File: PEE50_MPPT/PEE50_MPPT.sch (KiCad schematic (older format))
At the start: 46 parts, among them J1 PV_IN1, J2 PV_IN2, J3 Conn_01x02_Female, J4 Conn_01x02_Female, J5 PV_IN4, J6 PV_IN3, Q1 BC547, Q2 BC547, Q3 BC547, Q4 BC547, U1 LM3480-3.3

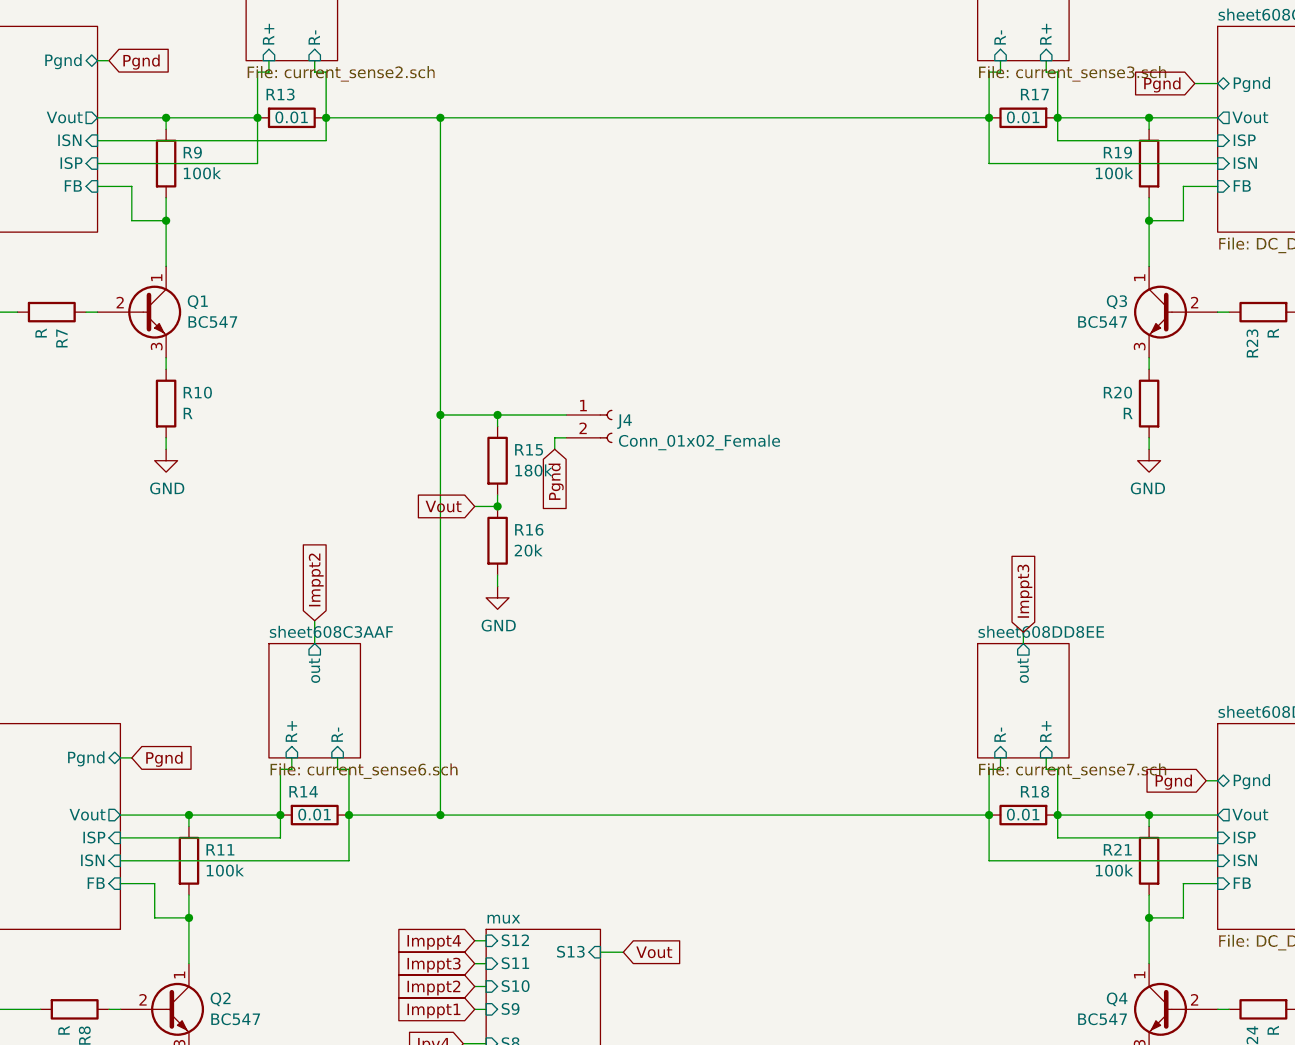
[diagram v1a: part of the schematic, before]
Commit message: best veel footprints ingevoegd
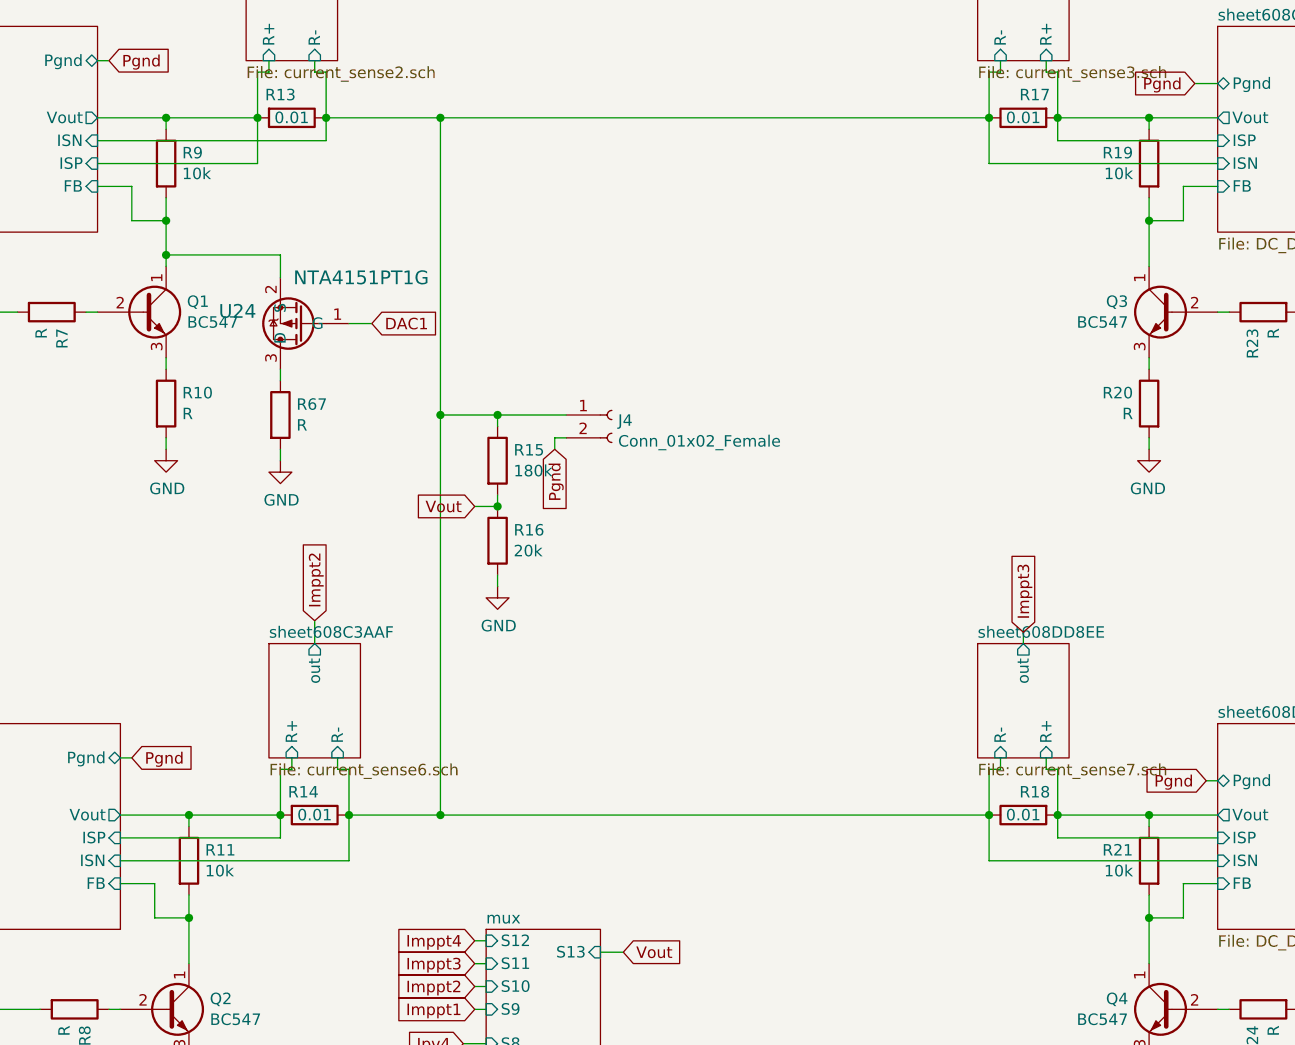
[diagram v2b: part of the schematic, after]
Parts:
- added R67: R, Resistor_SMD:R_1206_3216Metric_Pad1.42x1.75mm_HandSolder, symbol Device:R
- added U24: NTA4151PT1G, SOT416_463_ONS, symbol Robin_lib:NTA4151PT1G
- C1, C2, C57, C58: footprint (none) -> Capacitor_SMD:C_1206_3216Metric_Pad1.42x1.75mm_HandSolder
- JP1: footprint (none) -> Connector_PinHeader_2.54mm:PinHeader_1x03_P2.54mm_Vertical
- R1, R10, R12, R15, R16, R2, R20, R22, R23, R24, R27, R28, R29, R3, R30, R4, R7, R8: footprint (none) -> Resistor_SMD:R_1206_3216Metric_Pad1.42x1.75mm_HandSolder
- R11, R19, R21, R9: value 100k -> 10k; footprint (none) -> Resistor_SMD:R_1206_3216Metric_Pad1.42x1.75mm_HandSolder
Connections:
- net DAC1: now also U24.1 (G)
- net DC/DC_Converter/FB: now also U24.2 (S)
- net GND: now also R67.2
- new net: R67.1, U24.3 (D)
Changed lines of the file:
@@
 EESchema Schematic File Version 4
-LIBS:PEE50_MPPT-cache
-EELAYER 26 0
+EELAYER 30 0
 EELAYER END
 $Descr A4 11693 8268
@@
 P 2900 1950
 F 0 "R9" H 2970 1996 50  0000 L CNN
-F 1 "100k" H 2970 1905 50  0000 L CNN
-F 2 "" V 2830 1950 50  0001 C CNN
+F 1 "10k" H 2970 1905 50  0000 L CNN
+F 2 "Resistor_SMD:R_1206_3216Metric_Pad1.42x1.75mm_HandSolder" V 2830 1950 50  0001 C CNN
 F 3 "~" H 2900 1950 50  0001 C CNN
 	1    2900 1950
@@
 Connection ~ 2900 2200
 Wire Wire Line
-	2900 2200 2900 2400
+	2900 2200 2900 2350
 $Comp
 L Device:R R10
@@
 F 0 "R10" H 2970 3046 50  0000 L CNN
 F 1 "R" H 2970 2955 50  0000 L CNN
-F 2 "" V 2830 3000 50  0001 C CNN
+F 2 "Resistor_SMD:R_1206_3216Metric_Pad1.42x1.75mm_HandSolder" V 2830 3000 50  0001 C CNN
 F 3 "~" H 2900 3000 50  0001 C CNN
 	1    2900 3000
@@
 F 0 "R1" H 1020 2096 50  0000 L CNN
 F 1 "180k" H 1020 2005 50  0000 L CNN
-F 2 "" V 880 2050 50  0001 C CNN
+F 2 "Resistor_SMD:R_1206_3216Metric_Pad1.42x1.75mm_HandSolder" V 880 2050 50  0001 C CNN
 F 3 "~" H 950 2050 50  0001 C CNN
 	1    950  2050
@@
 F 0 "R2" H 1020 2446 50  0000 L CNN
 F 1 "20k" H 1020 2355 50  0000 L CNN
-F 2 "" V 880 2400 50  0001 C CNN
+F 2 "Resistor_SMD:R_1206_3216Metric_Pad1.42x1.75mm_HandSolder" V 880 2400 50  0001 C CNN
 F 3 "~" H 950 2400 50  0001 C CNN
 	1    950  2400
@@
 F 0 "R7" H 2470 2646 50  0000 L CNN
 F 1 "R" H 2470 2555 50  0000 L CNN
-F 2 "" V 2330 2600 50  0001 C CNN
+F 2 "Resistor_SMD:R_1206_3216Metric_Pad1.42x1.75mm_HandSolder" V 2330 2600 50  0001 C CNN
 F 3 "~" H 2400 2600 50  0001 C CNN
 	1    2400 2600
@@
 F 0 "R15" H 4420 3296 50  0000 L CNN
 F 1 "180k" H 4420 3205 50  0000 L CNN
-F 2 "" V 4280 3250 50  0001 C CNN
+F 2 "Resistor_SMD:R_1206_3216Metric_Pad1.42x1.75mm_HandSolder" V 4280 3250 50  0001 C CNN
 F 3 "~" H 4350 3250 50  0001 C CNN
 	1    4350 3250
@@
 F 0 "R16" H 4420 3646 50  0000 L CNN
 F 1 "20k" H 4420 3555 50  0000 L CNN
-F 2 "" V 4280 3600 50  0001 C CNN
+F 2 "Resistor_SMD:R_1206_3216Metric_Pad1.42x1.75mm_HandSolder" V 4280 3600 50  0001 C CNN
 F 3 "~" H 4350 3600 50  0001 C CNN
 	1    4350 3600
@@
 P 3000 5000
 F 0 "R11" H 3070 5046 50  0000 L CNN
-F 1 "100k" H 3070 4955 50  0000 L CNN
-F 2 "" V 2930 5000 50  0001 C CNN
+F 1 "10k" H 3070 4955 50  0000 L CNN
+F 2 "Resistor_SMD:R_1206_3216Metric_Pad1.42x1.75mm_HandSolder" V 2930 5000 50  0001 C CNN
 F 3 "~" H 3000 5000 50  0001 C CNN
 	1    3000 5000
@@
 F 0 "R12" H 3070 6096 50  0000 L CNN
 F 1 "R" H 3070 6005 50  0000 L CNN
-F 2 "" V 2930 6050 50  0001 C CNN
+F 2 "Resistor_SMD:R_1206_3216Metric_Pad1.42x1.75mm_HandSolder" V 2930 6050 50  0001 C CNN
 F 3 "~" H 3000 6050 50  0001 C CNN
 	1    3000 6050
@@
 F 0 "R3" H 1120 5146 50  0000 L CNN
 F 1 "180k" H 1120 5055 50  0000 L CNN
-F 2 "" V 980 5100 50  0001 C CNN
+F 2 "Resistor_SMD:R_1206_3216Metric_Pad1.42x1.75mm_HandSolder" V 980 5100 50  0001 C CNN
 F 3 "~" H 1050 5100 50  0001 C CNN
 	1    1050 5100
@@
 F 0 "R4" H 1120 5496 50  0000 L CNN
 F 1 "20k" H 1120 5405 50  0000 L CNN
-F 2 "" V 980 5450 50  0001 C CNN
+F 2 "Resistor_SMD:R_1206_3216Metric_Pad1.42x1.75mm_HandSolder" V 980 5450 50  0001 C CNN
 F 3 "~" H 1050 5450 50  0001 C CNN
 	1    1050 5450
@@
 F 0 "R8" H 2570 5696 50  0000 L CNN
 F 1 "R" H 2570 5605 50  0000 L CNN
-F 2 "" V 2430 5650 50  0001 C CNN
+F 2 "Resistor_SMD:R_1206_3216Metric_Pad1.42x1.75mm_HandSolder" V 2430 5650 50  0001 C CNN
 F 3 "~" H 2500 5650 50  0001 C CNN
 	1    2500 5650
@@
 P 7200 1950
 F 0 "R19" H 7270 1996 50  0000 L CNN
-F 1 "100k" H 7270 1905 50  0000 L CNN
-F 2 "" V 7130 1950 50  0001 C CNN
+F 1 "10k" H 7270 1905 50  0000 L CNN
+F 2 "Resistor_SMD:R_1206_3216Metric_Pad1.42x1.75mm_HandSolder" V 7130 1950 50  0001 C CNN
 F 3 "~" H 7200 1950 50  0001 C CNN
 	1    7200 1950
@@
 F 0 "R20" H 7270 3046 50  0000 L CNN
 F 1 "R" H 7270 2955 50  0000 L CNN
-F 2 "" V 7130 3000 50  0001 C CNN
+F 2 "Resistor_SMD:R_1206_3216Metric_Pad1.42x1.75mm_HandSolder" V 7130 3000 50  0001 C CNN
 F 3 "~" H 7200 3000 50  0001 C CNN
 	1    7200 3000
@@
 F 0 "R27" H 9220 2096 50  0000 L CNN
 F 1 "180k" H 9220 2005 50  0000 L CNN
-F 2 "" V 9080 2050 50  0001 C CNN
+F 2 "Resistor_SMD:R_1206_3216Metric_Pad1.42x1.75mm_HandSolder" V 9080 2050 50  0001 C CNN
 F 3 "~" H 9150 2050 50  0001 C CNN
 	1    9150 2050
@@
 F 0 "R28" H 9220 2446 50  0000 L CNN
 F 1 "20k" H 9220 2355 50  0000 L CNN
-F 2 "" V 9080 2400 50  0001 C CNN
+F 2 "Resistor_SMD:R_1206_3216Metric_Pad1.42x1.75mm_HandSolder" V 9080 2400 50  0001 C CNN
 F 3 "~" H 9150 2400 50  0001 C CNN
 	1    9150 2400
@@
 F 0 "R23" H 7770 2646 50  0000 L CNN
 F 1 "R" H 7770 2555 50  0000 L CNN
-F 2 "" V 7630 2600 50  0001 C CNN
+F 2 "Resistor_SMD:R_1206_3216Metric_Pad1.42x1.75mm_HandSolder" V 7630 2600 50  0001 C CNN
 F 3 "~" H 7700 2600 50  0001 C CNN
 	1    7700 2600
@@
 P 7200 5000
 F 0 "R21" H 7270 5046 50  0000 L CNN
-F 1 "100k" H 7270 4955 50  0000 L CNN
-F 2 "" V 7130 5000 50  0001 C CNN
+F 1 "10k" H 7270 4955 50  0000 L CNN
+F 2 "Resistor_SMD:R_1206_3216Metric_Pad1.42x1.75mm_HandSolder" V 7130 5000 50  0001 C CNN
 F 3 "~" H 7200 5000 50  0001 C CNN
 	1    7200 5000
@@
 F 0 "R22" H 7270 6096 50  0000 L CNN
 F 1 "R" H 7270 6005 50  0000 L CNN
-F 2 "" V 7130 6050 50  0001 C CNN
+F 2 "Resistor_SMD:R_1206_3216Metric_Pad1.42x1.75mm_HandSolder" V 7130 6050 50  0001 C CNN
 F 3 "~" H 7200 6050 50  0001 C CNN
 	1    7200 6050
@@
 F 0 "R29" H 9220 5146 50  0000 L CNN
 F 1 "180k" H 9220 5055 50  0000 L CNN
-F 2 "" V 9080 5100 50  0001 C CNN
+F 2 "Resistor_SMD:R_1206_3216Metric_Pad1.42x1.75mm_HandSolder" V 9080 5100 50  0001 C CNN
 F 3 "~" H 9150 5100 50  0001 C CNN
 	1    9150 5100
@@
 F 0 "R30" H 9220 5496 50  0000 L CNN
 F 1 "20k" H 9220 5405 50  0000 L CNN
-F 2 "" V 9080 5450 50  0001 C CNN
+F 2 "Resistor_SMD:R_1206_3216Metric_Pad1.42x1.75mm_HandSolder" V 9080 5450 50  0001 C CNN
 F 3 "~" H 9150 5450 50  0001 C CNN
 	1    9150 5450
@@
 F 0 "R24" H 7770 5696 50  0000 L CNN
 F 1 "R" H 7770 5605 50  0000 L CNN
-F 2 "" V 7630 5650 50  0001 C CNN
+F 2 "Resistor_SMD:R_1206_3216Metric_Pad1.42x1.75mm_HandSolder" V 7630 5650 50  0001 C CNN
 F 3 "~" H 7700 5650 50  0001 C CNN
 	1    7700 5650
@@
 F 0 "JP1" V 2046 7252 50  0000 L CNN
 F 1 "Jumper_NC_Dual" V 1955 7252 50  0000 L CNN
-F 2 "" H 2000 7150 50  0001 C CNN
+F 2 "Connector_PinHeader_2.54mm:PinHeader_1x03_P2.54mm_Vertical" H 2000 7150 50  0001 C CNN
 F 3 "~" H 2000 7150 50  0001 C CNN
 	1    2000 7150
@@
 F 0 "C1" H 2215 6846 50  0000 L CNN
 F 1 "1u" H 2215 6755 50  0000 L CNN
-F 2 "" H 2138 6650 50  0001 C CNN
+F 2 "Capacitor_SMD:C_1206_3216Metric_Pad1.42x1.75mm_HandSolder" H 2138 6650 50  0001 C CNN
 F 3 "~" H 2100 6800 50  0001 C CNN
 	1    2100 6800
@@
 F 0 "C2" H 2915 6846 50  0000 L CNN
 F 1 "100n" H 2915 6755 50  0000 L CNN
-F 2 "" H 2838 6650 50  0001 C CNN
+F 2 "Capacitor_SMD:C_1206_3216Metric_Pad1.42x1.75mm_HandSolder" H 2838 6650 50  0001 C CNN
 F 3 "~" H 2800 6800 50  0001 C CNN
 	1    2800 6800
@@
 F 0 "C57" H 1865 7646 50  0000 L CNN
 F 1 "1u" H 1865 7555 50  0000 L CNN
-F 2 "" H 1788 7450 50  0001 C CNN
+F 2 "Capacitor_SMD:C_1206_3216Metric_Pad1.42x1.75mm_HandSolder" H 1788 7450 50  0001 C CNN
 F 3 "~" H 1750 7600 50  0001 C CNN
 	1    1750 7600
@@
 F 0 "C58" H 2115 7646 50  0000 L CNN
 F 1 "100n" H 2115 7555 50  0000 L CNN
-F 2 "" H 2038 7450 50  0001 C CNN
+F 2 "Capacitor_SMD:C_1206_3216Metric_Pad1.42x1.75mm_HandSolder" H 2038 7450 50  0001 C CNN
 F 3 "~" H 2000 7600 50  0001 C CNN
 	1    2000 7600
@@
 	1    0    0    -1
 $EndComp
+$Comp
+L Robin_lib:NTA4151PT1G U24
+U 1 1 6095AD8A
+P 4200 2700
+F 0 "U24" H 5105 2597 60  0000 L CNN
+F 1 "NTA4151PT1G" H 4350 2450 60  0000 L CNN
+F 2 "SOT416_463_ONS" H 5000 2940 60  0001 C CNN
+F 3 "" H 4200 2700 60  0000 C CNN
+	1    4200 2700
+	-1   0    0    1
+$EndComp
+Wire Wire Line
+	3400 2450 3400 2350
+Wire Wire Line
+	3400 2350 2900 2350
+Connection ~ 2900 2350
+Wire Wire Line
+	2900 2350 2900 2400
+$Comp
+L Device:R R67
+U 1 1 6096B3EE
+P 3400 3050
+F 0 "R67" H 3470 3096 50  0000 L CNN
+F 1 "R" H 3470 3005 50  0000 L CNN
+F 2 "Resistor_SMD:R_1206_3216Metric_Pad1.42x1.75mm_HandSolder" V 3330 3050 50  0001 C CNN
+F 3 "~" H 3400 3050 50  0001 C CNN
+	1    3400 3050
+	1    0    0    -1
+$EndComp
+$Comp
+L power:GND #PWR0104
+U 1 1 6096B7C0
+P 3400 3250
+F 0 "#PWR0104" H 3400 3000 50  0001 C CNN
+F 1 "GND" H 3405 3077 50  0000 C CNN
+F 2 "" H 3400 3250 50  0001 C CNN
+F 3 "" H 3400 3250 50  0001 C CNN
+	1    3400 3250
+	1    0    0    -1
+$EndComp
+Wire Wire Line
+	3400 3250 3400 3200
+Wire Wire Line
+	3400 2900 3400 2850
+Text GLabel 3800 2650 2    50   Input ~ 0
+DAC1
+Wire Wire Line
+	3800 2650 3700 2650
 $EndSCHEMATC

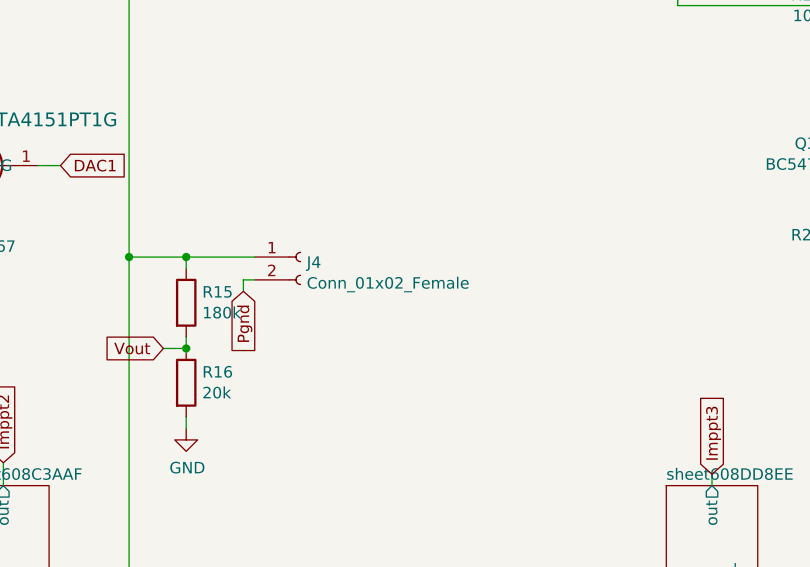
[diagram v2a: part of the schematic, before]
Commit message: footprints gemapt + 10x10 pcb rand getekend
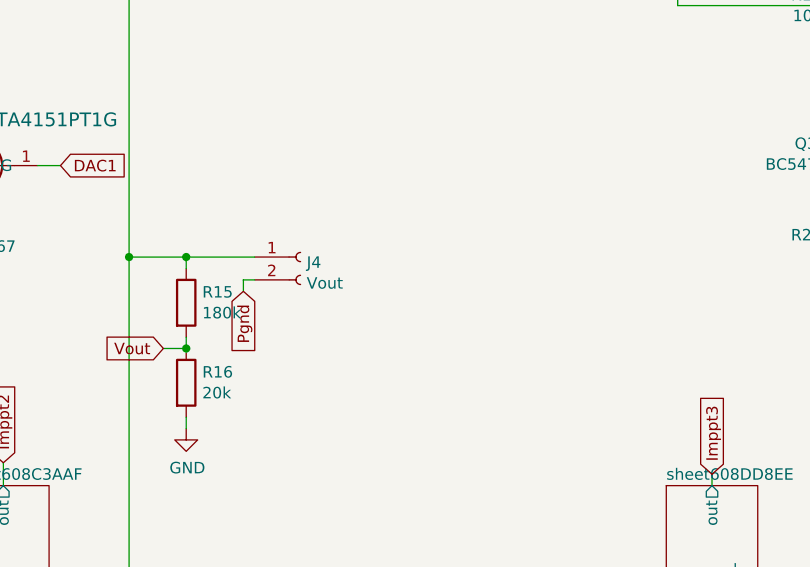
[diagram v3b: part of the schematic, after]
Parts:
- J1, J2, J5, J6: footprint (none) -> Connector_Phoenix_MSTB:PhoenixContact_MSTBA_2,5_2-G-5,08_1x02_P5.08mm_Horizontal
- J3: footprint (none) -> Connector_PinSocket_2.54mm:PinSocket_1x02_P2.54mm_Vertical
- J4: value Conn_01x02_Female -> Vout; footprint (none) -> Connector_Phoenix_MSTB:PhoenixContact_MSTBA_2,5_2-G-5,08_1x02_P5.08mm_Horizontal
- R13, R14, R17, R18, R25, R26, R5, R6: footprint (none) -> Resistor_SMD:R_2512_6332Metric_Pad1.52x3.35mm_HandSolder
- U24: footprint SOT416_463_ONS -> AudioProject:NTA4151PT1G
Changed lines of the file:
@@
 EESchema Schematic File Version 4
-EELAYER 30 0
+LIBS:PEE50_MPPT-cache
+EELAYER 26 0
 EELAYER END
 $Descr A4 11693 8268
@@
 F 0 "J1" H 594 1525 50  0000 C CNN
 F 1 "PV_IN1" H 594 1616 50  0000 C CNN
-F 2 "" H 700 1850 50  0001 C CNN
+F 2 "Connector_Phoenix_MSTB:PhoenixContact_MSTBA_2,5_2-G-5,08_1x02_P5.08mm_Horizontal" H 700 1850 50  0001 C CNN
 F 3 "~" H 700 1850 50  0001 C CNN
 	1    700  1850
@@
 F 0 "R5" V 1050 1700 50  0000 C CNN
 F 1 "0.01" V 1150 1750 50  0000 C CNN
-F 2 "" V 1080 1750 50  0001 C CNN
+F 2 "Resistor_SMD:R_2512_6332Metric_Pad1.52x3.35mm_HandSolder" V 1080 1750 50  0001 C CNN
 F 3 "~" H 1150 1750 50  0001 C CNN
 	1    1150 1750
@@
 F 0 "R13" V 3350 1700 50  0000 C CNN
 F 1 "0.01" V 3450 1750 50  0000 C CNN
-F 2 "" V 3380 1750 50  0001 C CNN
+F 2 "Resistor_SMD:R_2512_6332Metric_Pad1.52x3.35mm_HandSolder" V 3380 1750 50  0001 C CNN
 F 3 "~" H 3450 1750 50  0001 C CNN
 	1    3450 1750
@@
 P 4850 3050
 F 0 "J4" H 4877 3026 50  0000 L CNN
-F 1 "Conn_01x02_Female" H 4877 2935 50  0000 L CNN
-F 2 "" H 4850 3050 50  0001 C CNN
+F 1 "Vout" H 4877 2935 50  0000 L CNN
+F 2 "Connector_Phoenix_MSTB:PhoenixContact_MSTBA_2,5_2-G-5,08_1x02_P5.08mm_Horizontal" H 4850 3050 50  0001 C CNN
 F 3 "~" H 4850 3050 50  0001 C CNN
 	1    4850 3050
@@
 F 0 "J2" H 694 4575 50  0000 C CNN
 F 1 "PV_IN2" H 694 4666 50  0000 C CNN
-F 2 "" H 800 4900 50  0001 C CNN
+F 2 "Connector_Phoenix_MSTB:PhoenixContact_MSTBA_2,5_2-G-5,08_1x02_P5.08mm_Horizontal" H 800 4900 50  0001 C CNN
 F 3 "~" H 800 4900 50  0001 C CNN
 	1    800  4900
@@
 F 0 "R6" V 1150 4750 50  0000 C CNN
 F 1 "0.01" V 1250 4800 50  0000 C CNN
-F 2 "" V 1180 4800 50  0001 C CNN
+F 2 "Resistor_SMD:R_2512_6332Metric_Pad1.52x3.35mm_HandSolder" V 1180 4800 50  0001 C CNN
 F 3 "~" H 1250 4800 50  0001 C CNN
 	1    1250 4800
@@
 F 0 "R14" V 3450 4750 50  0000 C CNN
 F 1 "0.01" V 3550 4800 50  0000 C CNN
-F 2 "" V 3480 4800 50  0001 C CNN
+F 2 "Resistor_SMD:R_2512_6332Metric_Pad1.52x3.35mm_HandSolder" V 3480 4800 50  0001 C CNN
 F 3 "~" H 3550 4800 50  0001 C CNN
 	1    3550 4800
@@
 F 0 "J5" H 9294 1525 50  0000 C CNN
 F 1 "PV_IN4" H 9294 1616 50  0000 C CNN
-F 2 "" H 9400 1850 50  0001 C CNN
+F 2 "Connector_Phoenix_MSTB:PhoenixContact_MSTBA_2,5_2-G-5,08_1x02_P5.08mm_Horizontal" H 9400 1850 50  0001 C CNN
 F 3 "~" H 9400 1850 50  0001 C CNN
 	1    9400 1850
@@
 F 0 "R25" V 8850 1700 50  0000 C CNN
 F 1 "0.01" V 8950 1750 50  0000 C CNN
-F 2 "" V 8880 1750 50  0001 C CNN
+F 2 "Resistor_SMD:R_2512_6332Metric_Pad1.52x3.35mm_HandSolder" V 8880 1750 50  0001 C CNN
 F 3 "~" H 8950 1750 50  0001 C CNN
 	1    8950 1750
@@
 F 0 "R17" V 6550 1700 50  0000 C CNN
 F 1 "0.01" V 6650 1750 50  0000 C CNN
-F 2 "" V 6580 1750 50  0001 C CNN
+F 2 "Resistor_SMD:R_2512_6332Metric_Pad1.52x3.35mm_HandSolder" V 6580 1750 50  0001 C CNN
 F 3 "~" H 6650 1750 50  0001 C CNN
 	1    6650 1750
@@
 F 0 "J6" H 9294 4575 50  0000 C CNN
 F 1 "PV_IN3" H 9294 4666 50  0000 C CNN
-F 2 "" H 9400 4900 50  0001 C CNN
+F 2 "Connector_Phoenix_MSTB:PhoenixContact_MSTBA_2,5_2-G-5,08_1x02_P5.08mm_Horizontal" H 9400 4900 50  0001 C CNN
 F 3 "~" H 9400 4900 50  0001 C CNN
 	1    9400 4900
@@
 F 0 "R26" V 8850 4750 50  0000 C CNN
 F 1 "0.01" V 8950 4800 50  0000 C CNN
-F 2 "" V 8880 4800 50  0001 C CNN
+F 2 "Resistor_SMD:R_2512_6332Metric_Pad1.52x3.35mm_HandSolder" V 8880 4800 50  0001 C CNN
 F 3 "~" H 8950 4800 50  0001 C CNN
 	1    8950 4800
@@
 F 0 "R18" V 6550 4750 50  0000 C CNN
 F 1 "0.01" V 6650 4800 50  0000 C CNN
-F 2 "" V 6580 4800 50  0001 C CNN
+F 2 "Resistor_SMD:R_2512_6332Metric_Pad1.52x3.35mm_HandSolder" V 6580 4800 50  0001 C CNN
 F 3 "~" H 6650 4800 50  0001 C CNN
 	1    6650 4800
@@
 F 0 "J3" H 2477 7126 50  0000 L CNN
 F 1 "Conn_01x02_Female" H 2477 7035 50  0000 L CNN
-F 2 "" H 2450 7150 50  0001 C CNN
+F 2 "Connector_PinSocket_2.54mm:PinSocket_1x02_P2.54mm_Vertical" H 2450 7150 50  0001 C CNN
 F 3 "~" H 2450 7150 50  0001 C CNN
 	1    2450 7150
@@
 F 0 "U24" H 5105 2597 60  0000 L CNN
 F 1 "NTA4151PT1G" H 4350 2450 60  0000 L CNN
-F 2 "SOT416_463_ONS" H 5000 2940 60  0001 C CNN
+F 2 "AudioProject:NTA4151PT1G" H 5000 2940 60  0001 C CNN
 F 3 "" H 4200 2700 60  0000 C CNN
 	1    4200 2700

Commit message: best veel al gedaan voor 1e mppt
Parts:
- C1: footprint Capacitor_SMD:C_1206_3216Metric_Pad1.42x1.75mm_HandSolder -> AudioProject:CSD18543Q3A
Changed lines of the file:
@@
 F 0 "C1" H 2215 6846 50  0000 L CNN
 F 1 "1u" H 2215 6755 50  0000 L CNN
-F 2 "Capacitor_SMD:C_1206_3216Metric_Pad1.42x1.75mm_HandSolder" H 2138 6650 50  0001 C CNN
+F 2 "AudioProject:CSD18543Q3A" H 2138 6650 50  0001 C CNN
 F 3 "~" H 2100 6800 50  0001 C CNN
 	1    2100 6800
